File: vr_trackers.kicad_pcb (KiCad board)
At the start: 4 copper layers, 30 x 30 mm, 61 parts, among them SW2 TS-1088-AR02016, U1 nRF52840, U2 TPS63001DRCR, U3 MAX40203AUK+T, U4 MAX40203AUK+T, U5 LSM6DSVQTR, U6 BMM350_C17225907, U7 XL7EL89COI-111YLC-32M, U8 BQ24075RGTR, U9 MAX17048G+T10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

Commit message: Second revision of the pcb
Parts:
- removed the REF** at (38.5, 21.4)
- removed the REF** at (40.6, 24.6)
- moved C3 3.10 mm to (36.4, 27.3), turned to 0 degrees
- moved C2 2.39 mm to (34.1, 20.3)
- moved U7 2.14 mm to (35.1, 25.1)
- moved C4 1.78 mm to (34.5, 22.7)
- moved C12 1.44 mm to (36.8, 20.3), turned to 0 degrees
- moved U5 1.33 mm to (38.6, 24.8), turned to 0 degrees
- moved USB1 0.66 mm to (27.4, 37.1)
- moved C1 0.10 mm to (40.7, 21.1)
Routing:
- net /SPI_MISO: track 14.0 -> 17.7 mm
- net GND: track 83.4 -> 86.8 mm, vias 34 -> 71
- net /SPI_CS: track 23.3 -> 20.5 mm
- net /USB_VBUS: track 35.9 -> 38.6 mm
- net Net-(U1-XC1): track 5.33 -> 7.82 mm, vias 0 -> 2
- net Net-(U1-XC2): track 4.44 -> 6.88 mm, vias 0 -> 2
- net /POWER: track 36.4 -> 34.2 mm, vias 2 -> 3
- net /INT2: track 17.8 -> 19.7 mm
- net Net-(U1-ANT): track 11.2 -> 9.35 mm, vias 2 -> 0
- net /INT1: track 13.7 -> 15.4 mm
- net Net-(USB1-DP1): track 3.39 -> 4.79 mm
- net Net-(U1-DEC3): track 11.4 -> 10.4 mm
- net Net-(USB1-CC2): track 1.58 -> 2.24 mm
- net Net-(USB1-CC1): track 1.95 -> 2.49 mm
- removed copper zone on In2.Cu, net GND

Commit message: Fix errors
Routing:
- net GND: track 86.8 -> 85.1 mm, vias 71 -> 68
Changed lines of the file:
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@@
 	)
 	(segment
-		(start 33.74 32.4)
-		(end 33.74 32.5725)
-		(width 0.3)
-		(layer "F.Cu")
-		(net 2)
-	)
-	(segment
-		(start 30.605 33.03)
-		(end 30.075 32.5)
-		(width 0.3)
-		(layer "F.Cu")
-		(net 2)
-	)
-	(segment
 		(start 13.649 29.051)
 		(end 13.2 29.5)
@@
 	)
 	(segment
+		(start 33.74 33.235)
+		(end 31.725 35.25)
+		(width 0.3)
+		(layer "F.Cu")
+		(net 2)
+	)
+	(segment
 		(start 14.547501 32.15)
 		(end 15.297501 32.15)
@@
 	)
 	(segment
-		(start 33.74 32.5725)
-		(end 31.725 34.5875)
-		(width 0.3)
-		(layer "F.Cu")
-		(net 2)
-	)
-	(segment
 		(start 16.797501 32.9)
 		(end 17.4 32.9)
@@
 	)
 	(segment
+		(start 33.74 32.4)
+		(end 33.74 33.235)
+		(width 0.3)
+		(layer "F.Cu")
+		(net 2)
+	)
+	(segment
 		(start 17.34 36.65)
 		(end 17.34 37.012)
@@
 	)
 	(segment
-		(start 30.605 34.7)
-		(end 30.605 33.03)
-		(width 0.3)
-		(layer "F.Cu")
-		(net 2)
-	)
-	(segment
 		(start 36.4 29.7)
 		(end 36.249 29.549)
@@
 	)
 	(via
-		(at 21.9 38.3)
-		(size 0.6)
-		(drill 0.3)
-		(layers "F.Cu" "B.Cu")
-		(free yes)
-		(net 2)
-	)
-	(via
 		(at 41 33.2)
 		(size 0.6)
@@
 	)
 	(via
-		(at 25 38.45)
-		(size 0.6)
-		(drill 0.3)
-		(layers "F.Cu" "B.Cu")
-		(free yes)
-		(net 2)
-	)
-	(via
 		(at 24.6 40.7)
 		(size 0.6)
@@
 	)
 	(via
-		(at 19.5 20)
+		(at 31.3 33.7)
 		(size 0.6)
 		(drill 0.3)
@@
 	)
 	(via
-		(at 39.35 20.25)
+		(at 19.5 20)
 		(size 0.6)
 		(drill 0.3)
@@
 	)
 	(via
-		(at 23.5 33.5)
+		(at 39.35 20.25)
 		(size 0.6)
 		(drill 0.3)
@@
 	)
 	(via
-		(at 25.9 38.33)
+		(at 23.5 33.5)
 		(size 0.6)
 		(drill 0.3)
@@
 	)
 	(via
-		(at 24.6 39.21)
-		(size 0.6)
-		(drill 0.3)
-		(layers "F.Cu" "B.Cu")
-		(free yes)
-		(net 2)
-	)
-	(via
 		(at 32.31 26.24)
 		(size 0.6)
@@
 	)
 	(segment
-		(start 36.249 33.351)
-		(end 36.249 34.851)
+		(start 31.028232 38.151)
+		(end 32.949 38.151)
 		(width 0.2)
 		(layer "B.Cu")
@@
 	)
 	(segment
-		(start 33.4 38.625996)
-		(end 32.077496 39.9485)
+		(start 28.002 35.298)
+		(end 28.002 37.273621)
 		(width 0.2)
 		(layer "B.Cu")
@@
 	)
 	(segment
-		(start 28.002 35.298)
-		(end 28.002 37.273621)
+		(start 38.449 28.249)
+		(end 37.451 28.249)
 		(width 0.2)
 		(layer "B.Cu")
@@
 	)
 	(segment
-		(start 25.327121 39.9485)
-		(end 19.4485 39.9485)
+		(start 27.4485 39.9485)
+		(end 29.230732 39.9485)
 		(width 0.2)
 		(layer "B.Cu")
@@
 	)
 	(segment
-		(start 32.077496 39.9485)
-		(end 27.4485 39.9485)
+		(start 21.8 38.2)
+		(end 25.7 38.2)
 		(width 0.2)
 		(layer "B.Cu")
@@
 	)
 	(segment
-		(start 26.38781 38.88781)
-		(end 25.327121 39.9485)
+		(start 19.4485 39.9485)
+		(end 20.0515 39.9485)
 		(width 0.2)
 		(layer "B.Cu")
@@
 	)
 	(segment
-		(start 30.9 32.4)
-		(end 28.002 35.298)
+		(start 37.451 28.249)
+		(end 37.3 28.4)
 		(width 0.2)
 		(layer "B.Cu")
@@
 	)
 	(segment
-		(start 27.4485 39.9485)
-		(end 26.38781 38.88781)
+		(start 20.0515 39.9485)
+		(end 21.8 38.2)
+		(width 0.2)
+		(layer "B.Cu")
+		(net 31)
+	)
+	(segment
+		(start 30.9 32.4)
+		(end 28.002 35.298)
 		(width 0.2)
 		(layer "B.Cu")
@@
 	(segment
 		(start 36.249 34.851)
-		(end 33.4 37.7)
+		(end 36.249 33.351)
 		(width 0.2)
 		(layer "B.Cu")
@@
 	)
 	(segment
-		(start 28.002 37.273621)
+		(start 25.7 38.2)
 		(end 26.38781 38.88781)
 		(width 0.2)
@@
 	)
 	(segment
-		(start 38.8 30.8)
-		(end 36.249 33.351)
+		(start 15.05 35.2)
+		(end 15.05 35.55)
 		(width 0.2)
 		(layer "B.Cu")
@@
 	)
 	(segment
-		(start 37.451 28.249)
-		(end 38.449 28.249)
+		(start 29.230732 39.9485)
+		(end 31.028232 38.151)
 		(width 0.2)
 		(layer "B.Cu")
@@
 	)
 	(segment
-		(start 15.05 35.2)
-		(end 15.1 35.15)
+		(start 28.002 37.273621)
+		(end 26.38781 38.88781)
 		(width 0.2)
 		(layer "B.Cu")
@@
 	)
 	(segment
-		(start 33.4 37.7)
-		(end 33.4 38.625996)
+		(start 26.38781 38.88781)
+		(end 27.4485 39.9485)
 		(width 0.2)
 		(layer "B.Cu")
@@
 	)
 	(segment
-		(start 38.449 28.249)
-		(end 38.8 28.6)
+		(start 36.249 33.351)
+		(end 38.8 30.8)
 		(width 0.2)
 		(layer "B.Cu")
@@
 	)
 	(segment
-		(start 19.4485 39.9485)
-		(end 15.05 35.55)
+		(start 15.1 35.15)
+		(end 15.05 35.2)
 		(width 0.2)
 		(layer "B.Cu")
@@
 	)
 	(segment
-		(start 37.3 28.4)
-		(end 37.451 28.249)
+		(start 32.949 38.151)
+		(end 36.249 34.851)
 		(width 0.2)
 		(layer "B.Cu")
@@
 	)
 	(segment
-		(start 15.05 35.55)
-		(end 15.05 35.2)
+		(start 38.8 30.8)
+		(end 38.8 28.6)
 		(width 0.2)
 		(layer "B.Cu")
@@
 	(segment
 		(start 38.8 28.6)
-		(end 38.8 30.8)
+		(end 38.449 28.249)
+		(width 0.2)
+		(layer "B.Cu")
+		(net 31)
+	)
+	(segment
+		(start 15.05 35.55)
+		(end 19.4485 39.9485)
 		(width 0.2)
 		(layer "B.Cu")
@@
 	)
 	(segment
-		(start 31.037136 36.851)
-		(end 29.594 35.407864)
+		(start 31.451 32.171768)
+		(end 31.451 32.628232)
 		(width 0.2)
 		(layer "B.Cu")
@@
 	)
 	(segment
-		(start 33.451 36.528232)
-		(end 33.128232 36.851)
+		(start 30.879232 31.6)
+		(end 31.451 32.171768)
+		(width 0.2)
+		(layer "B.Cu")
+		(net 32)
+	)
+	(segment
+		(start 33.128232 36.851)
+		(end 33.451 36.528232)
 		(width 0.2)
 		(layer "B.Cu")
@@
 	)
 	(segment
-		(start 33.451 33.549)
-		(end 33.451 36.528232)
+		(start 30.123636 36.6)
+		(end 30.786136 36.6)
 		(width 0.2)
 		(layer "B.Cu")
@@
 	)
 	(segment
-		(start 33.128232 36.851)
-		(end 31.037136 36.851)
+		(start 29.8 31.6)
+		(end 27.651 33.749)
 		(width 0.2)
 		(layer "B.Cu")
@@
 	)
 	(segment
-		(start 29.8 31.6)
-		(end 27.651 33.749)
+		(start 33.451 33.549)
+		(end 38.2 28.8)
+		(width 0.2)
+		(layer "B.Cu")
+		(net 32)
+	)
+	(segment
+		(start 30.786136 36.6)
+		(end 31.037136 36.851)
 		(width 0.2)
 		(layer "B.Cu")
@@
 	(segment
 		(start 29.594 34.485232)
-		(end 31.451 32.628232)
+		(end 29.594 36.070364)
 		(width 0.2)
 		(layer "B.Cu")
@@
 	)
 	(segment
-		(start 31.451 32.628232)
-		(end 31.451 32.171768)
+		(start 33.451 36.528232)
+		(end 33.451 33.549)
 		(width 0.2)
 		(layer "B.Cu")
@@
 	)
 	(segment
-		(start 30.879232 31.6)
-		(end 29.8 31.6)
+		(start 29.594 36.070364)
+		(end 30.123636 36.6)
 		(width 0.2)
 		(layer "B.Cu")
@@
 	)
 	(segment
-		(start 29.594 35.407864)
+		(start 31.451 32.628232)
 		(end 29.594 34.485232)
 		(width 0.2)
@@
 	)
 	(segment
-		(start 31.451 32.171768)
-		(end 30.879232 31.6)
+		(start 31.037136 36.851)
+		(end 33.128232 36.851)
 		(width 0.2)
 		(layer "B.Cu")
@@
 	)
 	(segment
-		(start 38.2 28.8)
-		(end 33.451 33.549)
+		(start 29.8 31.6)
+		(end 30.879232 31.6)
 		(width 0.2)
 		(layer "B.Cu")

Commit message: Move the step file to a models directory
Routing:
- net GND: vias 68 -> 69
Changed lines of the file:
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@@
+	)
+	(via
+		(at 25.1 39.5)
+		(size 0.6)
+		(drill 0.3)
+		(layers "F.Cu" "B.Cu")
+		(free yes)
+		(net 2)
 	)
 	(via

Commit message: Add stuff i forget what
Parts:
- added REF**: ToolingHole_1.152mm, MountingHole:ToolingHole_1.152mm, F.Cu at (40.5, 13.5)
- moved C1 1.08 mm to (39.6, 21.1)
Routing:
- net GND: vias 69 -> 68
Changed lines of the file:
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@@
 		)
 	)
+	(footprint "MountingHole:ToolingHole_1.152mm"
+		(layer "F.Cu")
+		(at 40.5 13.5)
+		(descr "Tooling Hole 1.152mm, 1.3mm solder mask, JLCPCB specification, https://jlcpcb.com/help/article/How-to-add-tooling-holes-for-PCB-assembly-order")
+		(tags "mounting")
+		(property "Reference" "REF**"
+			(at 0 -1.5 0)
+			(layer "F.SilkS")
+			(hide yes)
+			(effects
+				(font
+					(size 1 1)
+					(thickness 0.15)
+				)
+			)
+		)
+		(property "Value" "ToolingHole_1.152mm"
+			(at 0 1.6 0)
+			(layer "F.Fab")
+			(effects
+				(font
+					(size 1 1)
+					(thickness 0.15)
+				)
+			)
+		)
+		(property "Datasheet" ""
+			(at 0 0 0)
+			(unlocked yes)
+			(layer "F.Fab")
+			(hide yes)
+			(effects
+				(font
+					(size 1.27 1.27)
+					(thickness 0.15)
+				)
+			)
+		)
+		(property "Description" ""
+			(at 0 0 0)
+			(unlocked yes)
+			(layer "F.Fab")
+			(hide yes)
+			(effects
+				(font
+					(size 1.27 1.27)
+					(thickness 0.15)
+				)
+			)
+		)
+		(attr exclude_from_pos_files exclude_from_bom)
+		(fp_circle
+			(center 0 0)
+			(end 0.7 0)
+			(stroke
+				(width 0.05)
+				(type solid)
+			)
+			(fill no)
+			(layer "F.CrtYd")
+		)
+		(fp_text user "${REFERENCE}"
+			(at 0 0 0)
+			(layer "F.Fab")
+			(effects
+				(font
+					(size 1 1)
+					(thickness 0.15)
+				)
+			)
+		)
+		(pad "" np_thru_hole circle
+			(at 0 0)
+			(size 1.152 1.152)
+			(drill 1.152)
+			(layers "*.Cu" "*.Mask")
+			(solder_mask_margin 0.074)
+		)
+		(zone
+			(net 0)
+			(net_name "")
+			(layers "F.Cu" "B.Cu" "In1.Cu" "In2.Cu")
+			(hatch edge 0.5)
+			(connect_pads
+				(clearance 0)
+			)
+			(min_thickness 0.25)
+			(filled_areas_thickness no)
+			(keepout
+				(tracks not_allowed)
+				(vias allowed)
+				(pads allowed)
+				(copperpour not_allowed)
+				(footprints not_allowed)
+			)
+			(placement
+				(enabled no)
+				(sheetname "")
+			)
+			(fill
+				(thermal_gap 0.5)
+				(thermal_bridge_width 0.5)
+			)
+			(polygon
+				(pts
+					(xy 41.2 13.5) (xy 41.179659 13.332479) (xy 41.119819 13.174694) (xy 41.023958 13.035814) (xy 40.897645 12.923911)
+					(xy 40.748223 12.845489) (xy 40.584376 12.805104) (xy 40.415624 12.805104) (xy 40.251777 12.845489)
+					(xy 40.102355 12.923911) (xy 39.976042 13.035814) (xy 39.880181 13.174694) (xy 39.820341 13.332479)
+					(xy 39.8 13.5) (xy 39.820341 13.667521) (xy 39.880181 13.825306) (xy 39.976042 13.964186) (xy 40.102355 14.076089)
+					(xy 40.251777 14.154511) (xy 40.415624 14.194896) (xy 40.584376 14.194896) (xy 40.748223 14.154511)
+					(xy 40.897645 14.076089) (xy 41.023958 13.964186) (xy 41.119819 13.825306) (xy 41.179659 13.667521)
+				)
+			)
+		)
+		(embedded_fonts no)
+	)
 	(footprint "Resistor_SMD:R_0402_1005Metric"
 		(layer "F.Cu")
@@
 	(footprint "Capacitor_SMD:C_0603_1608Metric"
 		(layer "F.Cu")
-		(at 40.7 21.05 90)
+		(at 39.625 21.05 90)
 		(descr "Capacitor SMD 0603 (1608 Metric), square (rectangular) end terminal, IPC-7351 nominal, (Body size source: IPC-SM-782 page 76, https://www.pcb-3d.com/wordpress/wp-content/uploads/ipc-sm-782a_amendment_1_and_2.pdf), generated with kicad-footprint-generator")
 		(tags "capacitor")
@@
 	)
 	(via
-		(at 39.14 21.42)
-		(size 0.6)
-		(drill 0.3)
-		(layers "F.Cu" "B.Cu")
-		(free yes)
-		(net 2)
-	)
-	(via
 		(at 41.1 39.95)
 		(size 0.6)
@@
 	)
 	(via
-		(at 39.35 20.25)
-		(size 0.6)
-		(drill 0.3)
-		(layers "F.Cu" "B.Cu")
-		(free yes)
-		(net 2)
-	)
-	(via
 		(at 23.5 33.5)
 		(size 0.6)
@@
 	)
 	(via
+		(at 40.975 20.275)
+		(size 0.6)
+		(drill 0.3)
+		(layers "F.Cu" "B.Cu")
+		(free yes)
+		(net 2)
+	)
+	(via
 		(at 32.31 26.24)
 		(size 0.6)
@@
 	)
 	(segment
-		(start 40.7 23.5)
-		(end 40.95 23.75)
-		(width 0.3)
-		(layer "F.Cu")
-		(net 4)
-	)
-	(segment
 		(start 40.45 30.25)
 		(end 41.15 30.95)
@@
 	)
 	(segment
-		(start 38 29.7)
-		(end 38.2 29.9)
+		(start 39.625 21.825)
+		(end 40.325 21.825)
 		(width 0.2)
 		(layer "F.Cu")
@@
 	)
 	(segment
-		(start 28 29.6375)
-		(end 28 30)
+		(start 38 29.7)
+		(end 38.2 29.9)
 		(width 0.2)
 		(layer "F.Cu")
@@
 	)
 	(segment
-		(start 40.7 21.825)
-		(end 40.7 23.5)
-		(width 0.3)
+		(start 28 29.6375)
+		(end 28 30)
+		(width 0.2)
 		(layer "F.Cu")
 		(net 4)
@@
 	)
 	(segment
+		(start 40.325 21.825)
+		(end 41 22.5)
+		(width 0.2)
+		(layer "F.Cu")
+		(net 4)
+	)
+	(segment
 		(start 29.85 22.3)
 		(end 29.8 22.25)
@@
 	)
 	(via
+		(at 41 22.5)
+		(size 0.6)
+		(drill 0.3)
+		(layers "F.Cu" "B.Cu")
+		(net 4)
+	)
+	(via
 		(at 30.25 30.35)
 		(size 0.6)
@@
 		(net 4)
 	)
-	(via
-		(at 40.95 23.75)
-		(size 0.6)
-		(drill 0.3)
-		(layers "F.Cu" "B.Cu")
-		(net 4)
-	)

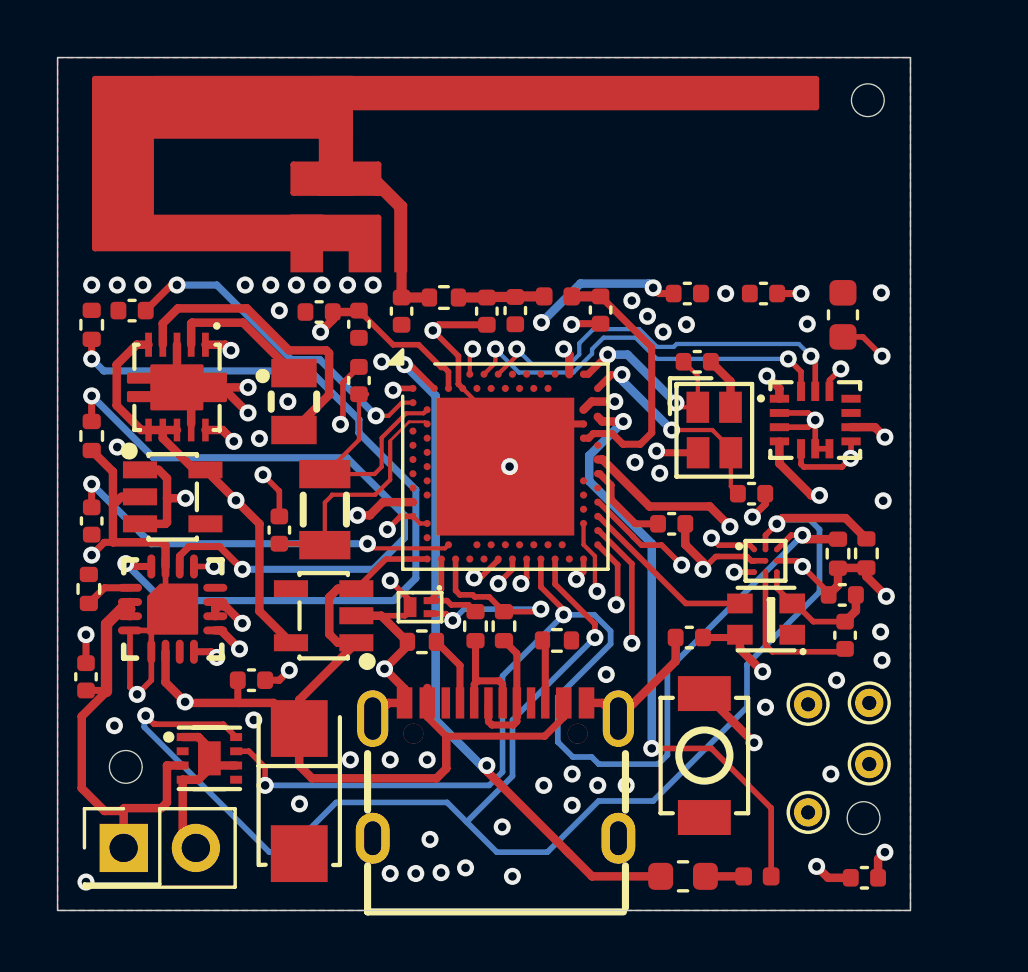
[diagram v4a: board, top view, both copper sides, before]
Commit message: add firmware stuff and update the pcb
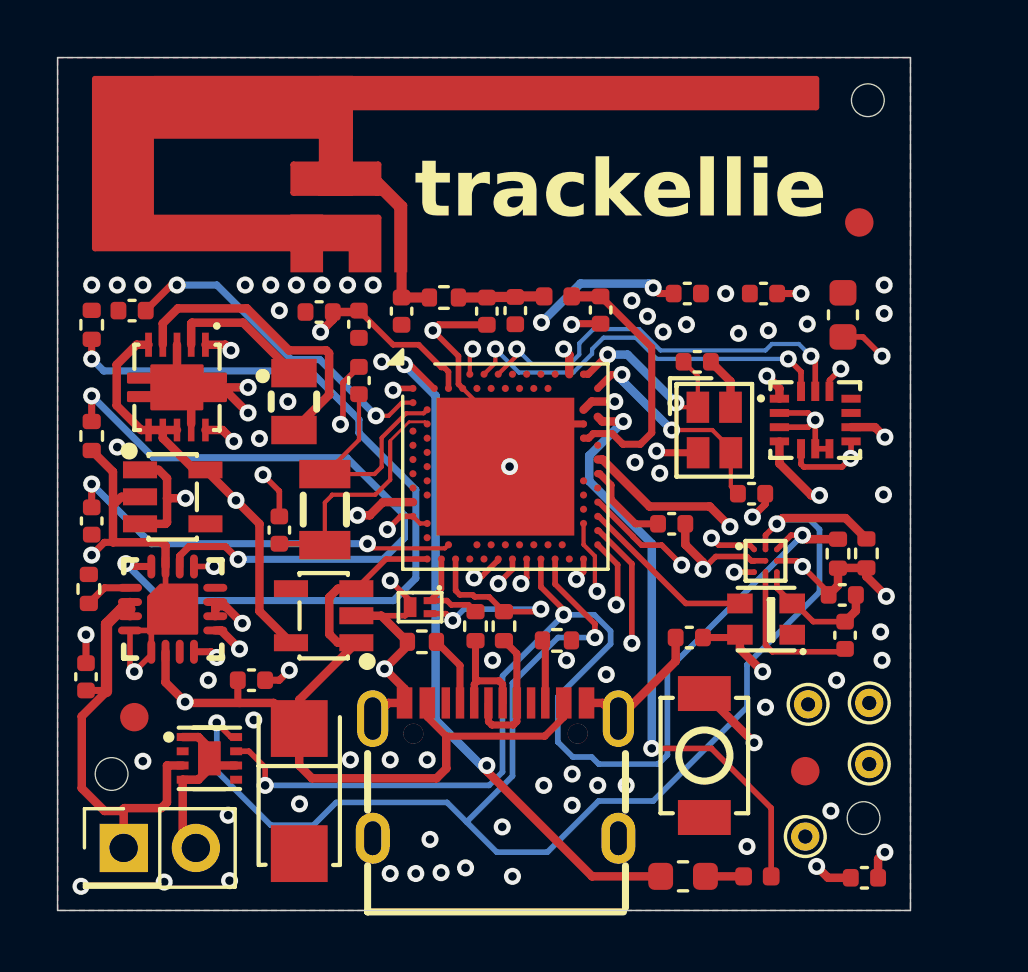
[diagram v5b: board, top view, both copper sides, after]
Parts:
- added REF**: Fiducial_1mm_Mask2mm, Fiducial:Fiducial_1mm_Mask2mm, F.Cu at (14.7, 35.2)
- added REF**: Fiducial_1mm_Mask2mm, Fiducial:Fiducial_1mm_Mask2mm, F.Cu at (38.3, 37.1)
- added REF**: Fiducial_1mm_Mask2mm, Fiducial:Fiducial_1mm_Mask2mm, F.Cu at (40.2, 17.8)
- moved TP3 0.86 mm to (38.3, 39.4)
- moved REF** 0.56 mm to (13.9, 37.2)
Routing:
- net /I2C_SDA: track 55.8 -> 51.3 mm
- net GND: track 85.1 -> 82.4 mm, vias 68 -> 78
- net /USB_VBUS: track 38.6 -> 37.7 mm
- net /BAT+: track 16.0 -> 15.1 mm
- net (no net): vias 0 -> 1
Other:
- board text added: "trackellie"

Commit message: Update the pcb to add a 4.5v lane, add a lot to the code, and make a second pcb to help programming
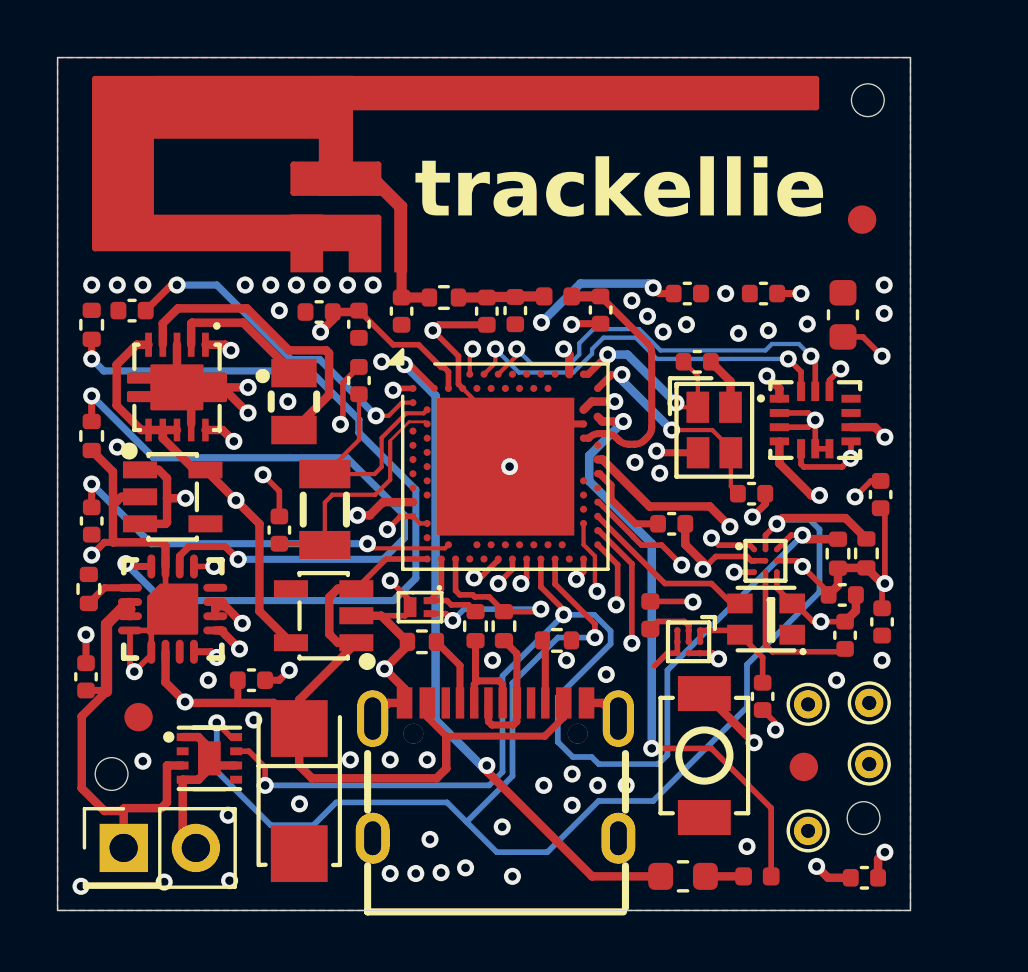
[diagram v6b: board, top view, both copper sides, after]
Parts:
- removed the REF** at (14.7, 35.2)
- removed the REF** at (38.3, 37.1)
- removed the REF** at (40.2, 17.8)
- added C21: 4.7uF, Capacitor_SMD:C_0402_1005Metric, F.Cu at (41.0, 27.4)
- added C24: 10uF, Capacitor_SMD:C_0402_1005Metric, F.Cu at (36.8, 34.5)
- added L5: 1uH, Inductor_SMD:L_0402_1005Metric, F.Cu at (32.9, 31.6)
- added REF**: Fiducial_1mm_Mask2mm, Fiducial:Fiducial_1mm_Mask2mm, F.Cu at (14.8, 35.2)
- added REF**: Fiducial_1mm_Mask2mm, Fiducial:Fiducial_1mm_Mask2mm, F.Cu at (40.3, 17.7)
- added REF**: Fiducial_1mm_Mask2mm, Fiducial:Fiducial_1mm_Mask2mm, F.Cu at (38.2, 37.0)
- added U10: TPS61254YFFR, easyeda2kicad:DSBGA-9_L1.3-W1.3-R3-C3-P0.40-BL, F.Cu at (34.2, 32.5)
- moved C20 6.80 mm to (41.0, 31.9), turned to 90 degrees
- moved TP3 0.22 mm to (38.4, 39.2)
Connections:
- LED1 pad 4: +3V3 -> /4V5
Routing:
- net /4V5: track 0.00 -> 3.88 mm
- net +3V3: track 22.9 -> 25.8 mm, vias 14 -> 15
- net Net-(L5-Pad2): track 0.00 -> 2.09 mm
- net GND: track 82.4 -> 82.5 mm, vias 78 -> 76
